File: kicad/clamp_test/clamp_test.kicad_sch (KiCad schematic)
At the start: 22 parts, among them J1 Conn_Coaxial, J2 Conn_Coaxial, J3 Conn_01x03_Pin, U1 LT1365CS

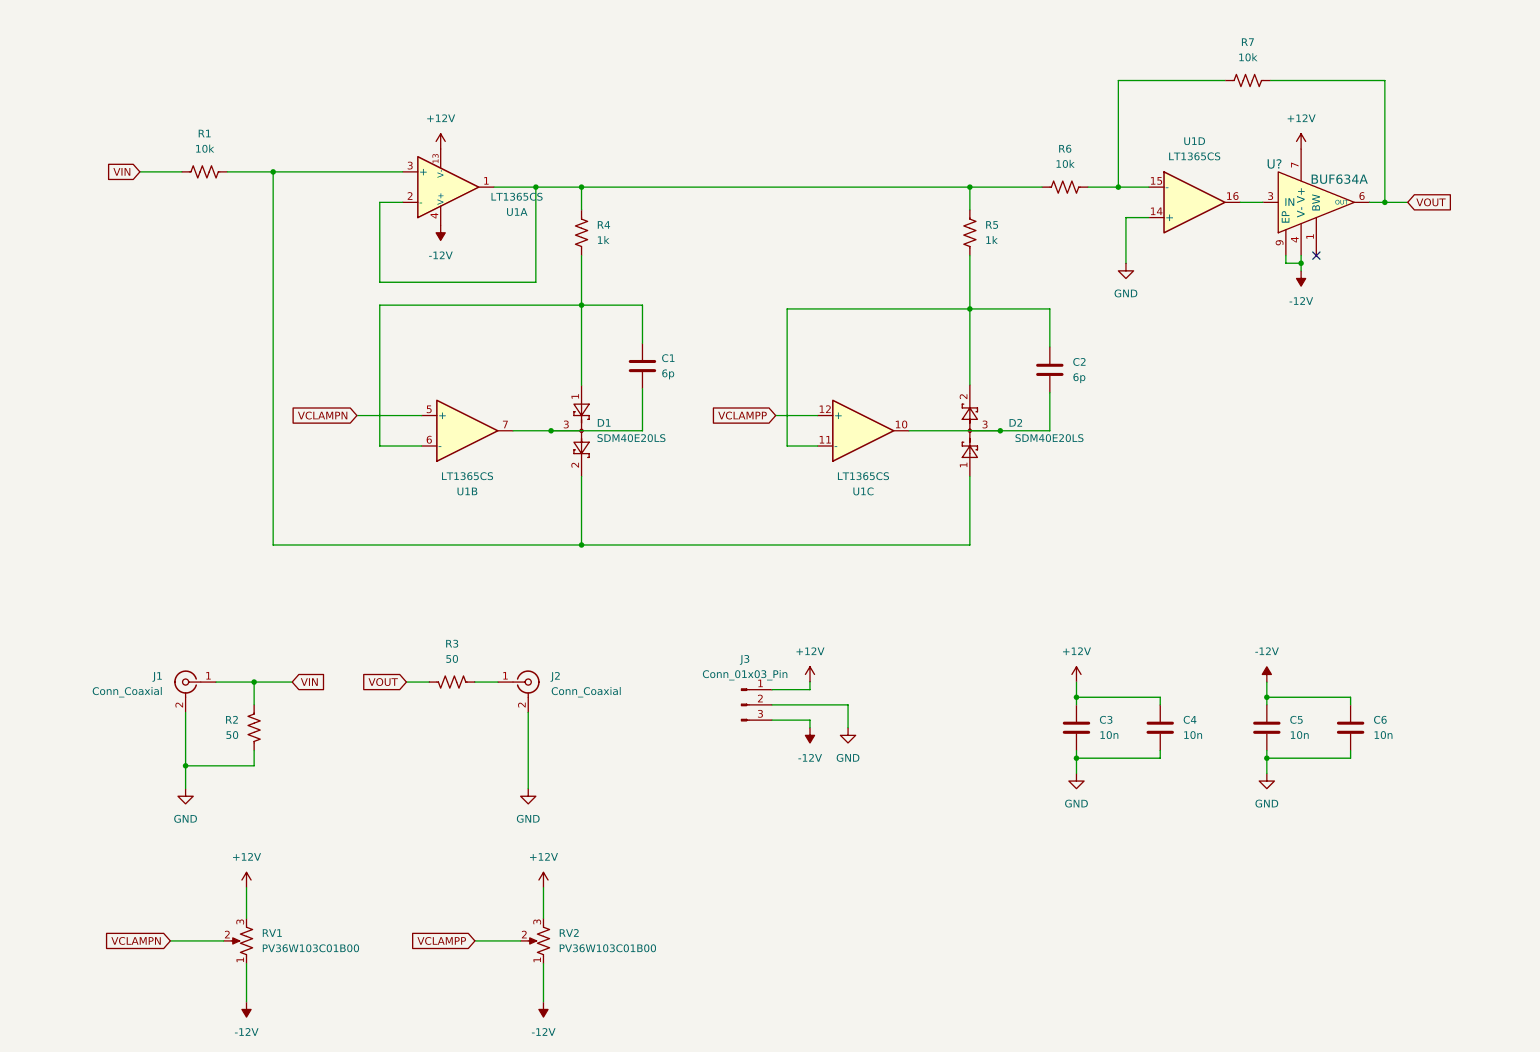
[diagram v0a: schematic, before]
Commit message: Changed buffer position
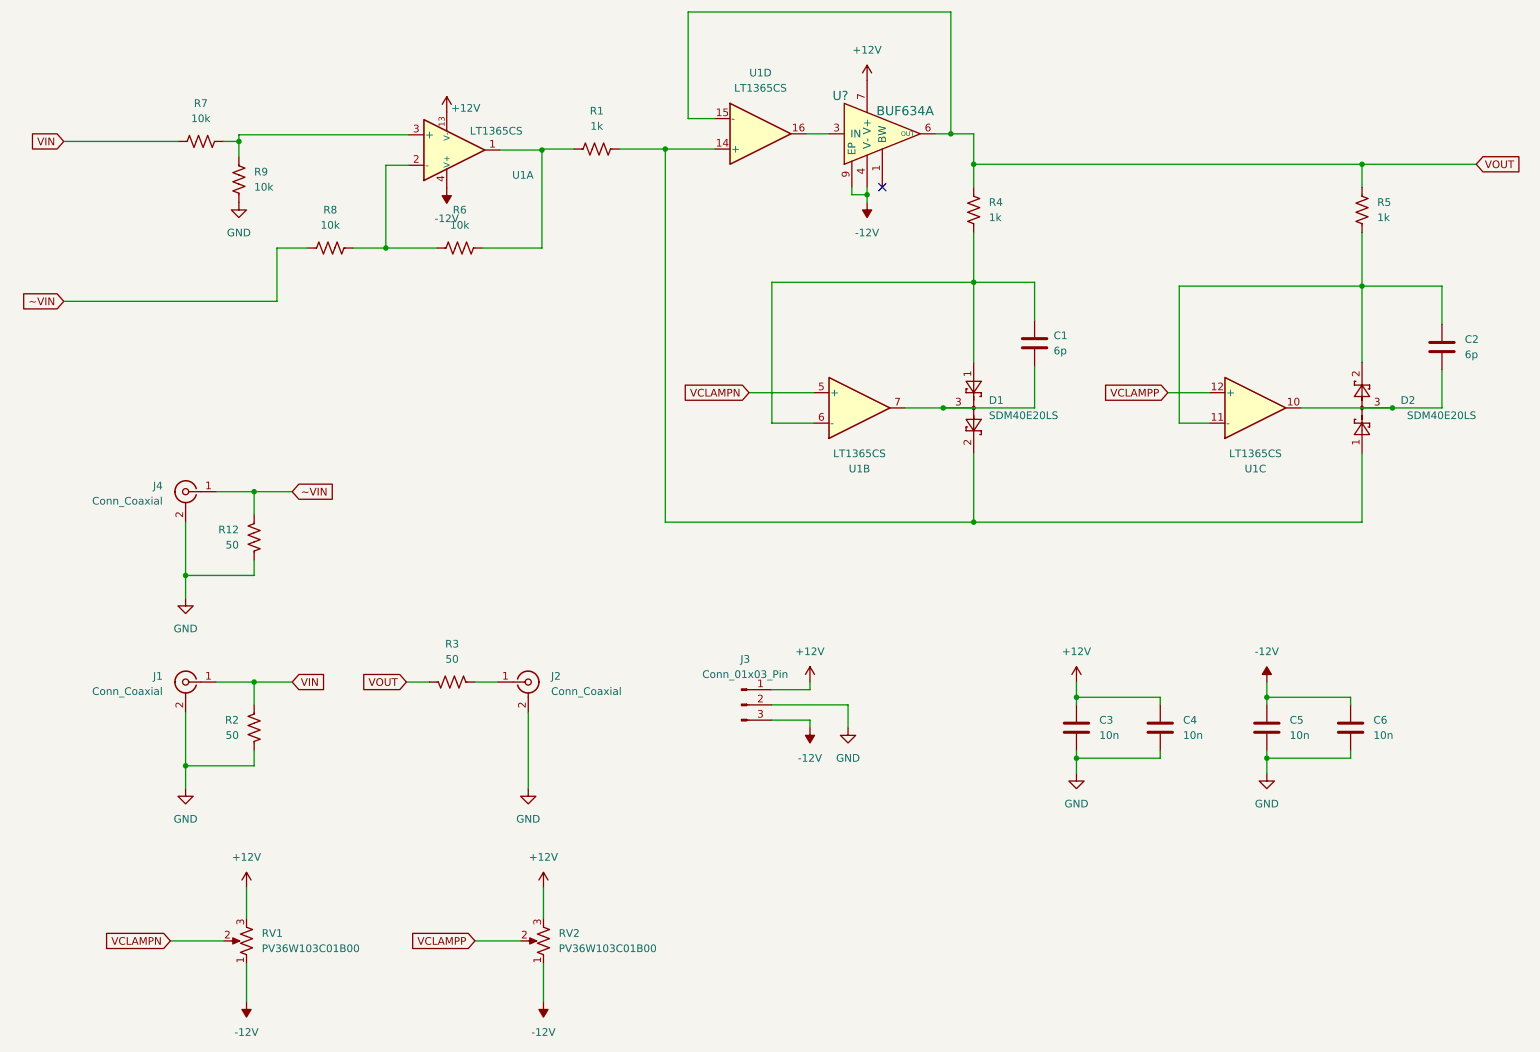
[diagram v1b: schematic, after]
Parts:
- added J4: Conn_Coaxial, Connector_Coaxial:SMA_Amphenol_132291_Vertical, symbol Connector:Conn_Coaxial
- added R12: 50, Resistor_SMD:R_0603_1608Metric, symbol Device:R_US
- added R8, R9: 10k, Resistor_SMD:R_0603_1608Metric, symbol Device:R_US
- R1: value 10k -> 1k
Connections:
- net GND: now also J4.2 (Ext), R12.2, R9.2; no longer U1.14 (+)
- net VIN: now also R7.2; no longer R1.1
- net VOUT: now also R4.2, R5.2, U1.15 (-); no longer R7.2
- net at D1.2, D2.1, R1.2: now also U1.14 (+); no longer U1.3 (+)
- new net: R7.1, R9.1, U1.3 (+)
- new net: R1.1, R6.1, U1.1
- new net: R6.2, R8.1, U1.2 (-)
- new net ~VIN: J4.1 (In), R12.1, R8.2
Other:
- moved on the sheet: C1, C2, D1, D2, R1, R4, R5, U1A, U1B, U1C, U1D, U?

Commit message: adjusted layout
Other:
- moved on the sheet: R6, R7, R8, U1A
